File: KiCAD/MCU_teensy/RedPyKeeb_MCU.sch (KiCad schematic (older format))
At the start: 7 parts, among them J0 Conn_01x04, J1 Conn_01x36, J2 Conn_01x04, U0 Teensy4.1, U1 TXS0104ED

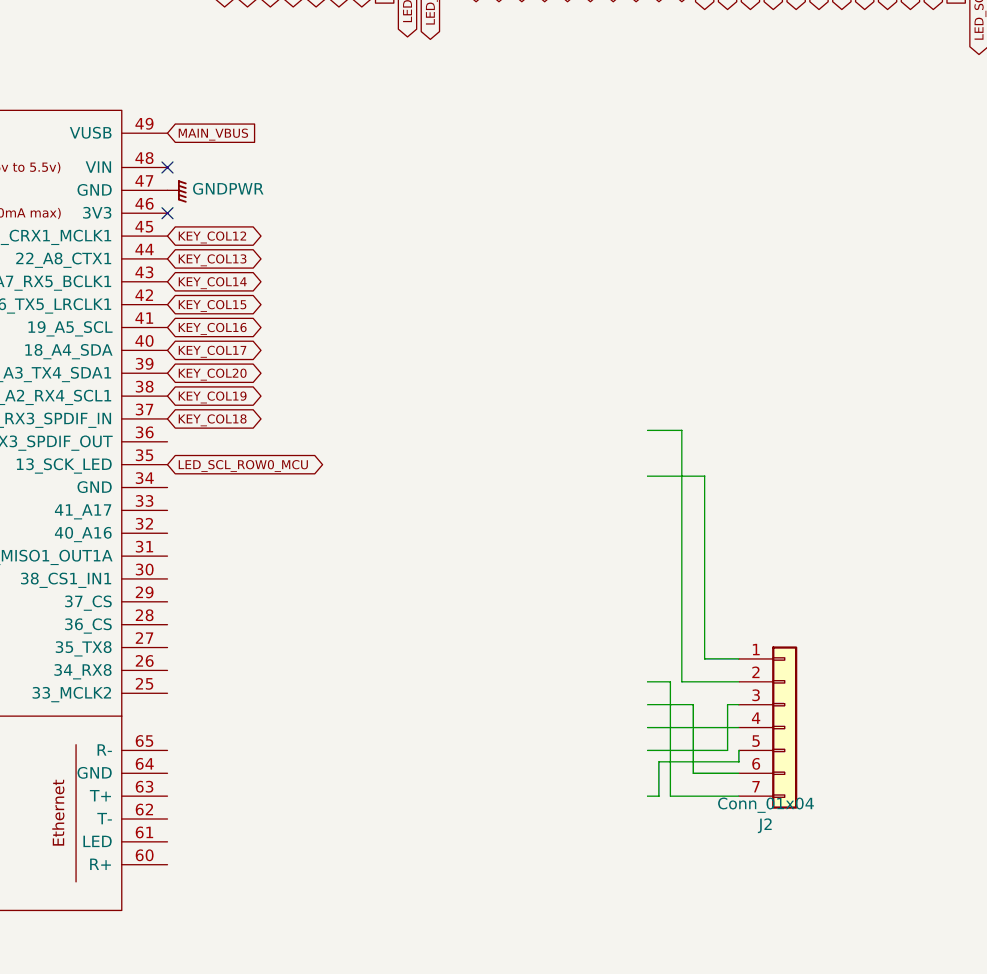
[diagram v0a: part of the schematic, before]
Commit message: Firmware is as-is for now, I've been testing PCB revisions and seeing what kind of latency I can poll the entire key matrix at KiCAD designs are looking really good now and I shoulld have parts in the next few weeks that will let me validate the keyboard as a whole plus the firmware.
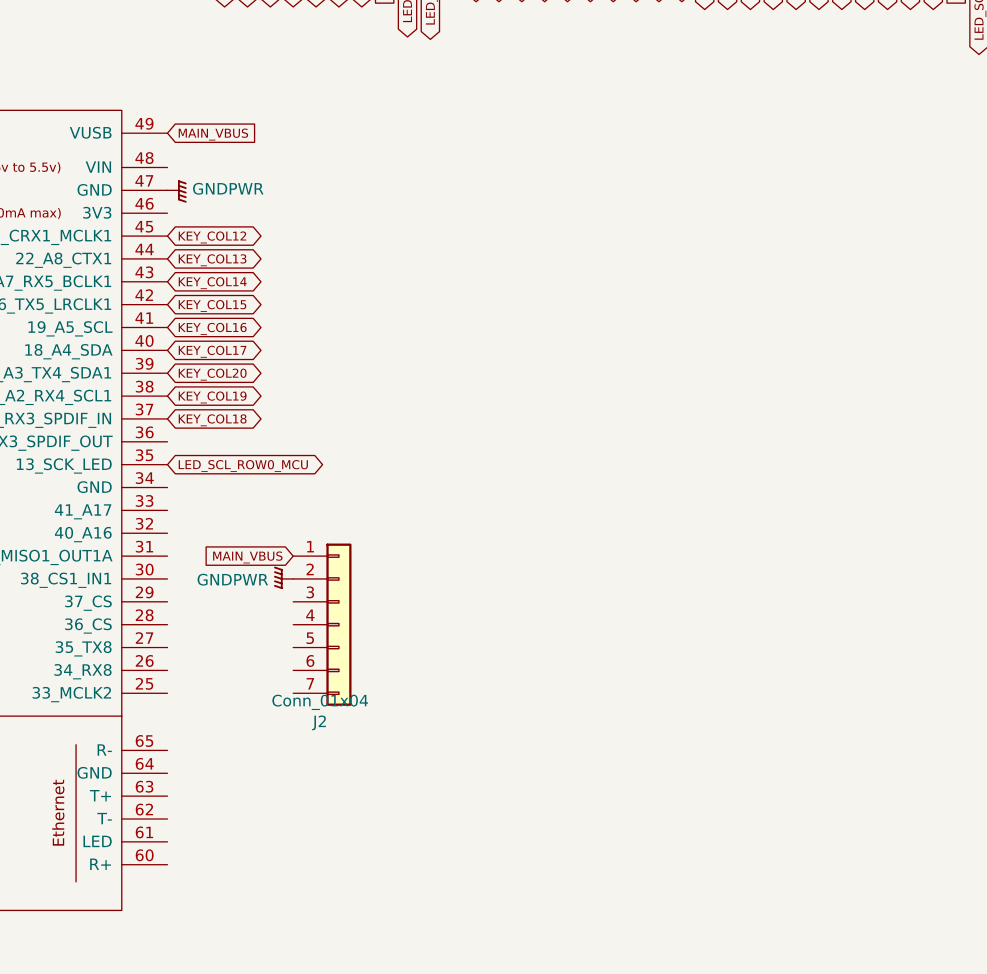
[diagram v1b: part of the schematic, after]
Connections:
- wire segments 28 -> 8
- no-connect marks 3 -> 1
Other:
- moved on the sheet: J2
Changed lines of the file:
@@
 L Connector_Generic:Conn_01x07 J2
 U 1 1 60E13064
-P 10000 4400
-F 0 "J2" H 9918 3975 50  0000 C CNN
-F 1 "Conn_01x04" H 9918 4066 50  0000 C CNN
-F 2 "Connector_JST:JST_EH_S7B-EH_1x07_P2.50mm_Horizontal" H 10000 4400 50  0001 C CNN
-F 3 "" H 10000 4400 50  0001 C CNN
-F 4 "485-3955" H 10000 4400 50  0001 C CNN "Mouser No"
-F 5 "1528-2751-ND" H 10000 4400 50  0001 C CNN "Digikey Part No"
-	1    10000 4400
-	1    0    0    -1
-$EndComp
-Wire Wire Line
-	9400 3100 9550 3100
-Wire Wire Line
-	9550 3100 9550 4200
-Wire Wire Line
-	9650 4100 9650 3300
-Wire Wire Line
-	9650 3300 9400 3300
-Wire Wire Line
-	9650 4100 9800 4100
-Wire Wire Line
-	9550 4200 9800 4200
-Wire Wire Line
-	9750 4500 9750 4300
-Wire Wire Line
-	9750 4300 9800 4300
-Wire Wire Line
-	9400 4400 9800 4400
-Wire Wire Line
-	9400 4500 9750 4500
-Wire Wire Line
-	9800 4500 9800 4550
-Wire Wire Line
-	9800 4550 9450 4550
-Wire Wire Line
-	9450 4550 9450 4700
-Wire Wire Line
-	9450 4700 9400 4700
-Wire Wire Line
-	9400 4300 9600 4300
-Wire Wire Line
-	9600 4300 9600 4600
-Wire Wire Line
-	9600 4600 9800 4600
-Wire Wire Line
-	9400 4200 9500 4200
-Wire Wire Line
-	9500 4200 9500 4700
-Wire Wire Line
-	9500 4700 9800 4700
+P 8050 3950
+F 0 "J2" H 7968 3525 50  0000 C CNN
+F 1 "Conn_01x04" H 7968 3616 50  0000 C CNN
+F 2 "Connector_JST:JST_EH_S7B-EH_1x07_P2.50mm_Horizontal" H 8050 3950 50  0001 C CNN
+F 3 "" H 8050 3950 50  0001 C CNN
+F 4 "485-3955" H 8050 3950 50  0001 C CNN "Mouser No"
+F 5 "1528-2751-ND" H 8050 3950 50  0001 C CNN "Digikey Part No"
+	1    8050 3950
+	1    0    0    -1
+$EndComp
 Text GLabel 5100 3150 0    39   BiDi ~ 0
 LED_SDA_ROW0_MCU
@@
 $EndComp
 NoConn ~ 5100 1950
-NoConn ~ 7300 2150
 Text GLabel 7300 3250 2    39   BiDi ~ 0
 LED_SCL_ROW0_MCU
@@
 Text GLabel 10950 850  3    39   BiDi ~ 0
 LED_SDA_STATUS0
-NoConn ~ 7300 1950
+Text GLabel 7850 3650 0    39   Input ~ 0
+MAIN_VBUS
+$Comp
+L power:GNDPWR #PWR0102
+U 1 1 60ACEAB9
+P 7850 3750
+F 0 "#PWR0102" H 7850 3550 50  0001 C CNN
+F 1 "GNDPWR" V 7855 3642 50  0000 R CNN
+F 2 "" H 7850 3700 50  0001 C CNN
+F 3 "" H 7850 3700 50  0001 C CNN
+	1    7850 3750
+	0    1    1    0
+$EndComp
 $EndSCHEMATC

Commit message: Latest KiCAD files and what ever I had for testing the old boards.
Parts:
- added R?: ERJ-6RED2003V, Resistors_SMD:R_0805_HandSoldering, symbol Device:R_Small_US
- J1: value Conn_01x36 -> Conn_02x20_Top_Bottom; footprint Connector_PinHeader_2.00mm:PinHeader_1x36_P2.00mm_Horizontal -> Connector_PinHeader_2.54mm:PinHeader_2x20_P2.54mm_Vertical; symbol conn:Conn_01x36 -> conn:Conn_02x20_Top_Bottom
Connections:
- net 33_REF: now also R?.2
- net GNDPWR: now also J1.35 (Pin_35), R?.1; no longer J1.11 (Pin_11)
- net KEY_COL0: now also J1.8 (Pin_8); no longer J1.12 (Pin_12)
- net KEY_COL1: now also J1.9 (Pin_9); no longer J1.13 (Pin_13)
- net KEY_COL10: now also J1.18 (Pin_18); no longer J1.22 (Pin_22)
- net KEY_COL11: now also J1.19 (Pin_19); no longer J1.23 (Pin_23)
- net KEY_COL12: now also J1.20 (Pin_20); no longer J1.24 (Pin_24)
- net KEY_COL13: now also J1.23 (Pin_23); no longer J1.25 (Pin_25)
- net KEY_COL14: now also J1.24 (Pin_24); no longer J1.26 (Pin_26)
- net KEY_COL15: now also J1.25 (Pin_25); no longer J1.27 (Pin_27)
- net KEY_COL16: now also J1.26 (Pin_26); no longer J1.28 (Pin_28)
- net KEY_COL17: now also J1.27 (Pin_27); no longer J1.29 (Pin_29)
- net KEY_COL18: now also J1.28 (Pin_28); no longer J1.30 (Pin_30)
- net KEY_COL19: now also J1.29 (Pin_29); no longer J1.31 (Pin_31)
- net KEY_COL2: now also J1.10 (Pin_10); no longer J1.14 (Pin_14)
- net KEY_COL20: now also J1.30 (Pin_30); no longer J1.32 (Pin_32)
- net KEY_COL3: now also J1.11 (Pin_11); no longer J1.15 (Pin_15)
- net KEY_COL4: now also J1.12 (Pin_12); no longer J1.16 (Pin_16)
- net KEY_COL5: now also J1.13 (Pin_13); no longer J1.17 (Pin_17)
- net KEY_COL6: now also J1.14 (Pin_14); no longer J1.18 (Pin_18)
- net KEY_COL7: now also J1.15 (Pin_15); no longer J1.19 (Pin_19)
- net KEY_COL8: now also J1.16 (Pin_16); no longer J1.20 (Pin_20)
- net KEY_COL9: now also J1.17 (Pin_17); no longer J1.21 (Pin_21)
- net LED_SCL_ROW0: now also J1.22 (Pin_22); no longer J1.9 (Pin_9)
- net LED_SCL_STATUS0: now also J1.40 (Pin_40); no longer J1.34 (Pin_34)
- net LED_SDA_ROW0: now also J1.21 (Pin_21); no longer J1.10 (Pin_10)
- net LED_SDA_STATUS0: now also J1.39 (Pin_39); no longer J1.35 (Pin_35)
- net MAIN_VBUS: now also J1.37 (Pin_37), J1.38 (Pin_38); no longer J1.33 (Pin_33), J1.8 (Pin_8)
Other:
- note added: "TODO: Power bus needs to be sorted, see Unified-Daughterboard?"
- note removed: "TODO: Power bus needs to be sorted, see Unified-Daughterboard?\n\nMCP23017_SO needs to have the interrupt pins (INT*)\nconfigured as not open-drain as the TXB0104D can't handle open-drain"
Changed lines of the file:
@@
 $EndDescr
 Text Notes 950  1100 0    59   ~ 0
-TODO: Power bus needs to be sorted, see Unified-Daughterboard?\n\nMCP23017_SO needs to have the interrupt pins (INT*)\nconfigured as not open-drain as the TXB0104D can't handle open-drain
+TODO: Power bus needs to be sorted, see Unified-Daughterboard?
 Text GLabel 7300 1800 2    39   Input ~ 0
 MAIN_VBUS
@@
 KEY_ROW6
 $Comp
-L conn:Conn_01x36 J1
+L conn:Conn_02x20_Top_Bottom J1
 U 1 1 609288FA
-P 9250 650
-F 0 "J1" V 9467 596 50  0000 C CNN
-F 1 "Conn_01x36" V 9376 596 50  0000 C CNN
-F 2 "Connector_PinHeader_2.00mm:PinHeader_1x36_P2.00mm_Horizontal" H 9250 650 50  0001 C CNN
-F 3 "~" H 9250 650 50  0001 C CNN
-	1    9250 650
-	0    -1   -1   0
-$EndComp
-Text GLabel 8050 850  3    39   BiDi ~ 0
+P 9200 1550
+F 0 "J1" V 9417 1496 50  0000 C CNN
+F 1 "Conn_02x20_Top_Bottom" V 9326 1496 50  0000 C CNN
+F 2 "Connector_PinHeader_2.54mm:PinHeader_2x20_P2.54mm_Vertical" H 9200 1550 50  0001 C CNN
+F 3 "~" H 9200 1550 50  0001 C CNN
+	1    9200 1550
+	0    -1   -1   0
+$EndComp
+Text GLabel 8800 1750 3    39   BiDi ~ 0
 KEY_ROW5
-Text GLabel 7950 850  3    39   BiDi ~ 0
+Text GLabel 8700 1750 3    39   BiDi ~ 0
 KEY_ROW4
-Text GLabel 7850 850  3    39   BiDi ~ 0
+Text GLabel 8600 1750 3    39   BiDi ~ 0
 KEY_ROW3
-Text GLabel 7750 850  3    39   BiDi ~ 0
+Text GLabel 8500 1750 3    39   BiDi ~ 0
 KEY_ROW2
-Text GLabel 7650 850  3    39   BiDi ~ 0
+Text GLabel 8400 1750 3    39   BiDi ~ 0
 KEY_ROW1
-Text GLabel 7550 850  3    39   BiDi ~ 0
+Text GLabel 8300 1750 3    39   BiDi ~ 0
 KEY_ROW0
-Text GLabel 8150 850  3    39   BiDi ~ 0
+Text GLabel 8900 1750 3    39   BiDi ~ 0
 KEY_ROW6
-Text GLabel 10650 850  3    39   BiDi ~ 0
+Text GLabel 9200 1250 1    39   BiDi ~ 0
 KEY_COL20
-Text GLabel 10050 850  3    39   BiDi ~ 0
+Text GLabel 8600 1250 1    39   BiDi ~ 0
 KEY_COL14
-Text GLabel 10150 850  3    39   BiDi ~ 0
+Text GLabel 8700 1250 1    39   BiDi ~ 0
 KEY_COL15
-Text GLabel 10250 850  3    39   BiDi ~ 0
+Text GLabel 8800 1250 1    39   BiDi ~ 0
 KEY_COL16
-Text GLabel 10350 850  3    39   BiDi ~ 0
+Text GLabel 8900 1250 1    39   BiDi ~ 0
 KEY_COL17
-Text GLabel 10450 850  3    39   BiDi ~ 0
+Text GLabel 9000 1250 1    39   BiDi ~ 0
 KEY_COL18
-Text GLabel 10550 850  3    39   BiDi ~ 0
+Text GLabel 9100 1250 1    39   BiDi ~ 0
 KEY_COL19
-Text GLabel 9950 850  3    39   BiDi ~ 0
+Text GLabel 8500 1250 1    39   BiDi ~ 0
 KEY_COL13
-Text GLabel 9850 850  3    39   BiDi ~ 0
+Text GLabel 10200 1750 3    39   BiDi ~ 0
 KEY_COL12
-Text GLabel 9750 850  3    39   BiDi ~ 0
+Text GLabel 10100 1750 3    39   BiDi ~ 0
 KEY_COL11
-Text GLabel 9650 850  3    39   BiDi ~ 0
+Text GLabel 10000 1750 3    39   BiDi ~ 0
 KEY_COL10
-Text GLabel 9550 850  3    39   BiDi ~ 0
+Text GLabel 9900 1750 3    39   BiDi ~ 0
 KEY_COL9
-Text GLabel 9450 850  3    39   BiDi ~ 0
+Text GLabel 9800 1750 3    39   BiDi ~ 0
 KEY_COL8
-Text GLabel 9350 850  3    39   BiDi ~ 0
+Text GLabel 9700 1750 3    39   BiDi ~ 0
 KEY_COL7
-Text GLabel 9250 850  3    39   BiDi ~ 0
+Text GLabel 9600 1750 3    39   BiDi ~ 0
 KEY_COL6
-Text GLabel 9150 850  3    39   BiDi ~ 0
+Text GLabel 9500 1750 3    39   BiDi ~ 0
 KEY_COL5
-Text GLabel 9050 850  3    39   BiDi ~ 0
+Text GLabel 9400 1750 3    39   BiDi ~ 0
 KEY_COL4
-Text GLabel 8950 850  3    39   BiDi ~ 0
+Text GLabel 9300 1750 3    39   BiDi ~ 0
 KEY_COL3
-Text GLabel 8850 850  3    39   BiDi ~ 0
+Text GLabel 9200 1750 3    39   BiDi ~ 0
 KEY_COL2
-Text GLabel 8750 850  3    39   BiDi ~ 0
+Text GLabel 9100 1750 3    39   BiDi ~ 0
 KEY_COL1
-Text GLabel 8650 850  3    39   BiDi ~ 0
+Text GLabel 9000 1750 3    39   BiDi ~ 0
 KEY_COL0
-Text GLabel 8450 850  3    39   BiDi ~ 0
+Text GLabel 8300 1250 1    39   BiDi ~ 0
 LED_SDA_ROW0
-Text GLabel 8350 850  3    39   BiDi ~ 0
+Text GLabel 8400 1250 1    39   BiDi ~ 0
 LED_SCL_ROW0
 $Comp
 L power:GNDPWR #PWR0105
 U 1 1 61B1080E
-P 8550 850
-F 0 "#PWR0105" H 8550 650 50  0001 C CNN
-F 1 "GNDPWR" H 8554 696 50  0000 C CNN
-F 2 "" H 8550 800 50  0001 C CNN
-F 3 "" H 8550 800 50  0001 C CNN
-	1    8550 850
-	1    0    0    -1
-$EndComp
-Text GLabel 8250 850  3    39   Input ~ 0
+P 9700 1250
+F 0 "#PWR0105" H 9700 1050 50  0001 C CNN
+F 1 "GNDPWR" H 9704 1096 50  0000 C CNN
+F 2 "" H 9700 1200 50  0001 C CNN
+F 3 "" H 9700 1200 50  0001 C CNN
+	1    9700 1250
+	-1   0    0    1
+$EndComp
+Text GLabel 9900 1250 1    39   Input ~ 0
 MAIN_VBUS
 $Comp
 L power:GNDPWR #PWR0115
 U 1 1 61B808C8
-P 11050 850
-F 0 "#PWR0115" H 11050 650 50  0001 C CNN
-F 1 "GNDPWR" H 11054 696 50  0000 C CNN
-F 2 "" H 11050 800 50  0001 C CNN
-F 3 "" H 11050 800 50  0001 C CNN
-	1    11050 850
-	1    0    0    -1
-$EndComp
-Text GLabel 10750 850  3    39   Input ~ 0
+P 9800 1250
+F 0 "#PWR0115" H 9800 1050 50  0001 C CNN
+F 1 "GNDPWR" H 9804 1096 50  0000 C CNN
+F 2 "" H 9800 1200 50  0001 C CNN
+F 3 "" H 9800 1200 50  0001 C CNN
+	1    9800 1250
+	-1   0    0    1
+$EndComp
+Text GLabel 10000 1250 1    39   Input ~ 0
 MAIN_VBUS
 $Comp
@@
 F 1 "TXS0104ED" H 2650 2110 50  0000 C CNN
 F 2 "Package_SO:SOIC-14_3.9x8.7mm_P1.27mm" H 2650 2150 50  0001 C CNN
-F 3 "http://www.ti.com/lit/ds/symlink/txb0104.pdf" H 2760 2995 50  0001 C CNN
+F 3 "https://www.ti.com/lit/ds/symlink/txs0104e.pdf" H 2760 2995 50  0001 C CNN
 F 4 "595-TXS0104ED" H 2650 2900 50  0001 C CNN "Mouser No"
 F 5 "TXS0104ED" H 2650 2900 50  0001 C CNN "element14 code"
@@
 	0    -1   -1   0
 $EndComp
-Wire Wire Line
-	2750 3700 3050 3700
-Wire Wire Line
-	3050 3700 3150 3700
-Connection ~ 3050 3700
-Wire Wire Line
-	3050 3400 3050 3700
 $Comp
 L Device:C C2
@@
 Text GLabel 5100 4050 0    39   BiDi ~ 0
 KEY_COL9
-Text GLabel 10850 850  3    39   BiDi ~ 0
+Text GLabel 10200 1250 1    39   BiDi ~ 0
 LED_SCL_STATUS0
-Text GLabel 10950 850  3    39   BiDi ~ 0
+Text GLabel 10100 1250 1    39   BiDi ~ 0
 LED_SDA_STATUS0
 Text GLabel 7850 3650 0    39   Input ~ 0
@@
 	0    1    1    0
 $EndComp
+$Comp
+L Device:R_Small_US R?
+U 1 1 60EF0352
+P 3300 3400
+F 0 "R?" V 3187 3400 50  0000 C CNN
+F 1 "ERJ-6RED2003V" H 3368 3355 50  0001 L CNN
+F 2 "Resistors_SMD:R_0805_HandSoldering" H 3300 3400 50  0001 C CNN
+F 3 "~" H 3300 3400 50  0001 C CNN
+F 4 "667-ERJ-6RED2003V" H 3300 3400 50  0001 C CNN "Mouser No"
+	1    3300 3400
+	0    1    1    0
+$EndComp
+Wire Wire Line
+	2750 3700 3150 3700
+$Comp
+L power:GNDPWR #PWR?
+U 1 1 60EF50AA
+P 3400 3400
+F 0 "#PWR?" H 3400 3200 50  0001 C CNN
+F 1 "GNDPWR" V 3405 3292 50  0000 R CNN
+F 2 "" H 3400 3350 50  0001 C CNN
+F 3 "" H 3400 3350 50  0001 C CNN
+	1    3400 3400
+	0    -1   -1   0
+$EndComp
+Text GLabel 3400 3500 2    39   Input ~ 0
+33_REF
+Wire Wire Line
+	3200 3500 3200 3400
+Wire Wire Line
+	3200 3500 3400 3500
+Wire Wire Line
+	3200 3400 3050 3400
+Connection ~ 3200 3400
 $EndSCHEMATC

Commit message: Minimum viable product! I still need to work out a few things on the PCBs but its finally real!
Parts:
- J1: footprint Connector_PinHeader_2.54mm:PinHeader_2x20_P2.54mm_Vertical -> Connector_PinSocket_2.54mm:PinSocket_2x20_P2.54mm_Vertical_SMD; Mouser No (none) -> 649-95278-102-40LF
- U0: Mouser No (none) -> 474-DEV-16771
- gave numbers to parts that had none: 1
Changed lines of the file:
@@
 F 0 "J1" V 9417 1496 50  0000 C CNN
 F 1 "Conn_02x20_Top_Bottom" V 9326 1496 50  0000 C CNN
-F 2 "Connector_PinHeader_2.54mm:PinHeader_2x20_P2.54mm_Vertical" H 9200 1550 50  0001 C CNN
+F 2 "Connector_PinSocket_2.54mm:PinSocket_2x20_P2.54mm_Vertical_SMD" H 9200 1550 50  0001 C CNN
 F 3 "~" H 9200 1550 50  0001 C CNN
+F 4 "649-95278-102-40LF" H 9200 1550 50  0001 C CNN "Mouser No"
 	1    9200 1550
 	0    -1   -1   0
@@
 F 2 "Custom_pico:Teensy41" H 5800 4500 50  0001 C CNN
 F 3 "" H 5800 4500 50  0001 C CNN
+F 4 "474-DEV-16771" H 6200 4100 50  0001 C CNN "Mouser No"
 	1    6200 4100
 	1    0    0    -1
@@
 $EndComp
 $Comp
-L Device:R_Small_US R?
+L Device:R_Small_US R1
 U 1 1 60EF0352
 P 3300 3400
-F 0 "R?" V 3187 3400 50  0000 C CNN
+F 0 "R1" V 3187 3400 50  0000 C CNN
 F 1 "ERJ-6RED2003V" H 3368 3355 50  0001 L CNN
 F 2 "Resistors_SMD:R_0805_HandSoldering" H 3300 3400 50  0001 C CNN
@@
 	2750 3700 3150 3700
 $Comp
-L power:GNDPWR #PWR?
+L power:GNDPWR #PWR0103
 U 1 1 60EF50AA
 P 3400 3400
-F 0 "#PWR?" H 3400 3200 50  0001 C CNN
+F 0 "#PWR0103" H 3400 3200 50  0001 C CNN
 F 1 "GNDPWR" V 3405 3292 50  0000 R CNN
 F 2 "" H 3400 3350 50  0001 C CNN
